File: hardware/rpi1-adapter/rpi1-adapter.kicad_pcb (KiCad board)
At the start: 2 copper layers, 17 x 35 mm, 17 parts, among them P1 I2C, P2 CONN_02X13, P3 UART, P4 CONN_02X08, P5 relays, P6 5V, U1 OPTO-TRANSISTOR-4, U2 OPTO-TRANSISTOR-4

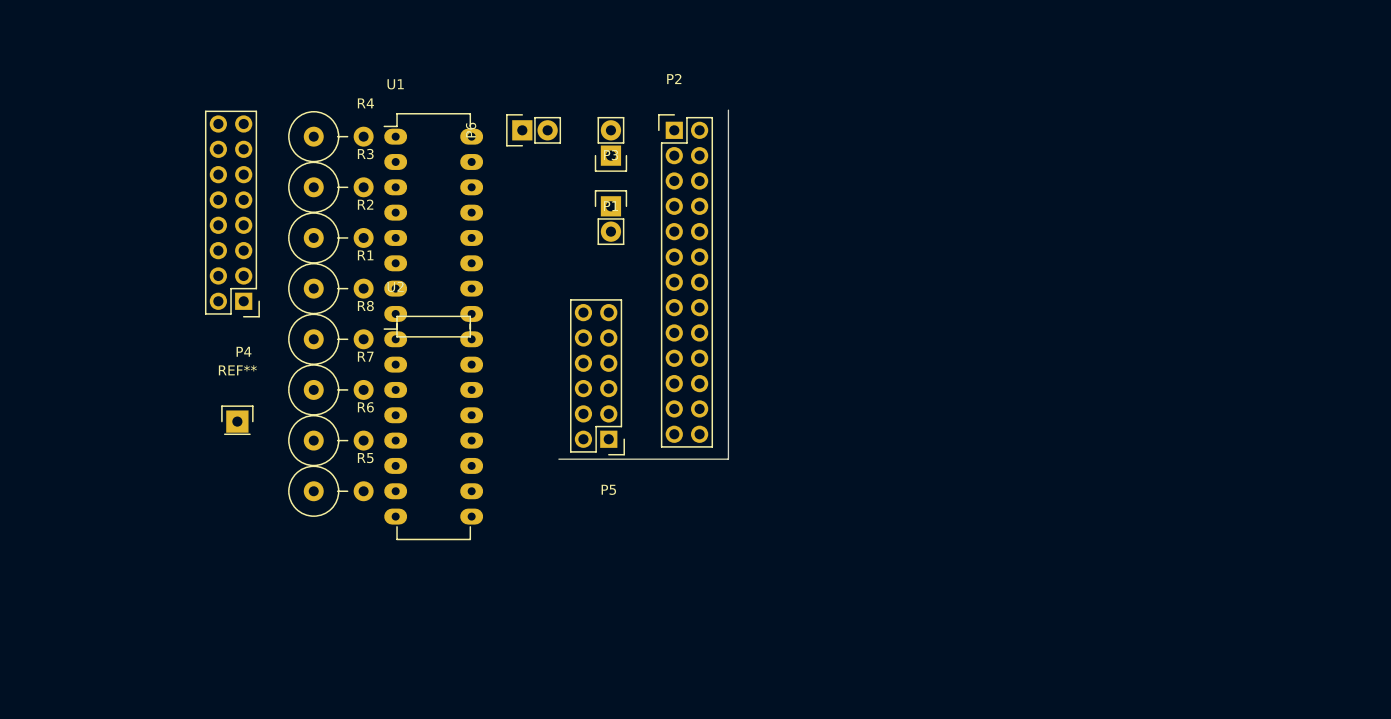
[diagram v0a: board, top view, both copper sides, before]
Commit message: o more on adapter. Add DC/DC converter to only need one 12V supply.
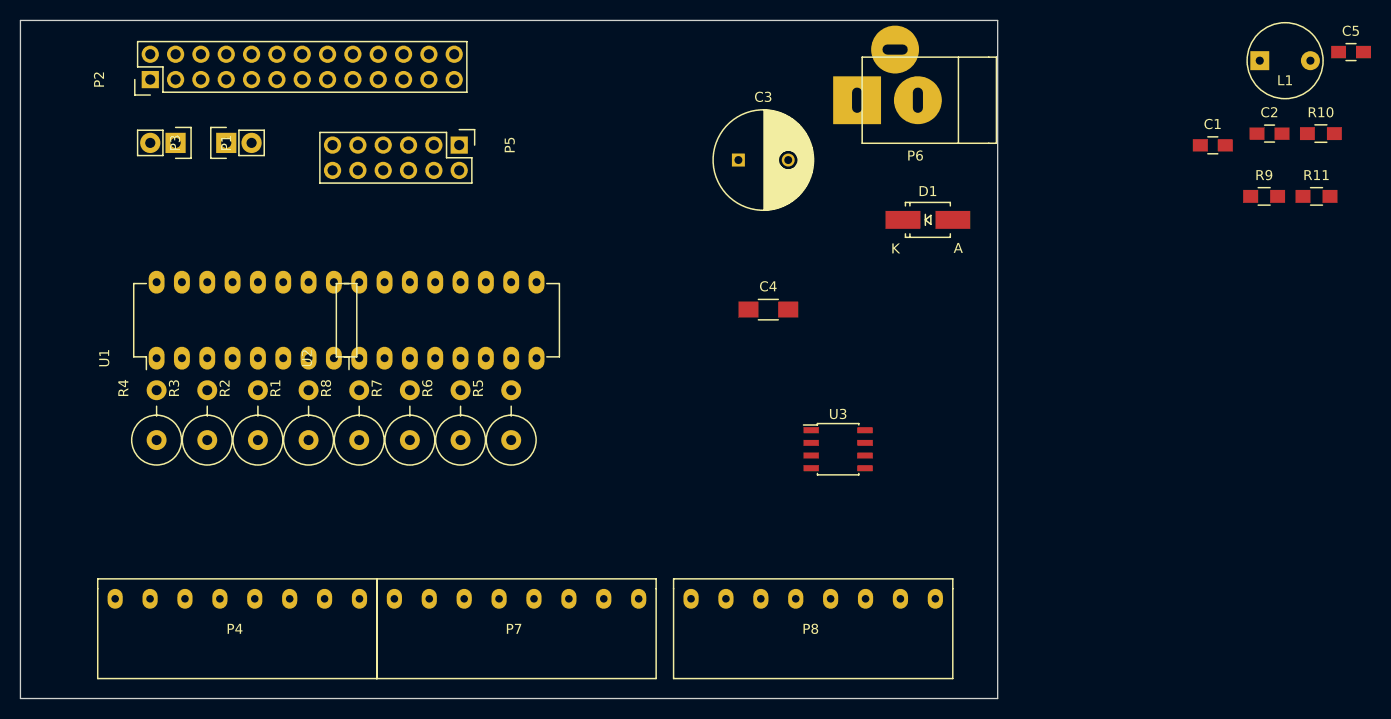
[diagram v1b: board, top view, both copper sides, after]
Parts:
- removed REF**: Pin_Header_Straight_1x01, Pin_Headers:Pin_Header_Straight_1x01
- added C1: 110p, Capacitors_SMD:C_0805_HandSoldering, F.Cu at (169.6, 34.5)
- added C2: 100n, Capacitors_SMD:C_0805_HandSoldering, F.Cu at (175.3, 33.3)
- added C3: 100u, Capacitors_ThroughHole:C_Radial_D10_L16_P5, F.Cu at (122.0, 36.0)
- added C4: 100u, Capacitors_SMD:C_1206_HandSoldering, F.Cu at (125.0, 51.0)
- added C5: 100n, Capacitors_SMD:C_0805_HandSoldering, F.Cu at (183.4, 25.2)
- added D1: D_Schottky_Small, Diodes_SMD:Diode-SMA_Handsoldering, F.Cu at (141.0, 42.0)
- added L1: L_Small, Inductors:INDUCTOR_V, F.Cu at (176.8, 26.0)
- added P7: CONN_01X08, terminal:TerminalBlock-8pin-3.5mm, F.Cu at (99.8, 80.0)
- added P8: CONN_01X08, terminal:TerminalBlock-8pin-3.5mm, F.Cu at (129.5, 80.0)
- added R10: 1k, Resistors_SMD:R_0805_HandSoldering, F.Cu at (180.4, 33.3)
- added R11: 3k, Resistors_SMD:R_0805_HandSoldering, F.Cu at (180.0, 39.6)
- added R9: 0R3, Resistors_SMD:R_0805_HandSoldering, F.Cu at (174.7, 39.6)
- added U3: MC34063, Housings_SOIC:SOIC-8_3.9x4.9mm_Pitch1.27mm, F.Cu at (132.0, 65.0)
- P4: value CONN_02X08 -> CONN_01X08; footprint Pin_Headers:Pin_Header_Straight_2x08 -> terminal:TerminalBlock-8pin-3.5mm
- P6: value 5V -> 12V; footprint Pin_Headers:Pin_Header_Straight_1x02 -> Connect:JACK_ALIM
- moved P2 52.8 mm to (63.0, 27.9), turned to 90 degrees
- moved P1 43.7 mm to (65.6, 34.3), turned to 270 degrees
- moved P6 39.8 mm to (140.0, 30.0), turned to 180 degrees
- moved P3 39.1 mm to (70.6, 34.3), turned to 90 degrees
- moved R4 33.4 mm to (63.7, 61.6), turned to 90 degrees
- moved P5 33.1 mm to (94.0, 34.5), turned to 270 degrees
- moved U1 32.7 mm to (63.7, 55.9), turned to 90 degrees
- moved P4 29.8 mm to (71.8, 80.0), turned to 0 degrees
- moved R3 26.4 mm to (68.7, 61.6), turned to 90 degrees
- moved R2 19.5 mm to (73.8, 61.6), turned to 90 degrees
- moved R5 18.9 mm to (99.2, 61.6), turned to 90 degrees
- moved R1 13.0 mm to (78.9, 61.6), turned to 90 degrees
- moved R6 12.5 mm to (94.1, 61.6), turned to 90 degrees
- moved R8 7.88 mm to (84.0, 61.6), turned to 90 degrees
- moved R7 7.57 mm to (89.1, 61.6), turned to 90 degrees
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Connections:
- P4 pad 1: Net-(P4-Pad1) -> GND
- P4 pad 2: GND -> Net-(P4-Pad2)
- P4 pad 3: Net-(P4-Pad3) -> GND
- P4 pad 4: GND -> Net-(P4-Pad4)
- P4 pad 5: Net-(P4-Pad5) -> GND
- P4 pad 6: GND -> Net-(P4-Pad6)
- P4 pad 7: Net-(P4-Pad7) -> GND
- P4 pad 8: GND -> Net-(P4-Pad8)
- P6 pad 2: +5V -> +12V
- U1 pad 1: Net-(R4-Pad2) -> Net-(R5-Pad2)
- U1 pad 10: in-17 -> in-4
- U1 pad 12: in-4 -> in-21
- U1 pad 14: in-21 -> in-22
- U1 pad 16: in-22 -> in-17
- U1 pad 2: Net-(P4-Pad15) -> Net-(P7-Pad8)
- U1 pad 3: Net-(R3-Pad2) -> Net-(R6-Pad2)
- U1 pad 4: Net-(P4-Pad13) -> Net-(P7-Pad6)
- U1 pad 5: Net-(R2-Pad2) -> Net-(R7-Pad2)
- U1 pad 6: Net-(P4-Pad11) -> Net-(P7-Pad4)
- U1 pad 7: Net-(R1-Pad2) -> Net-(R8-Pad2)
- U1 pad 8: Net-(P4-Pad9) -> Net-(P7-Pad2)
- U2 pad 1: Net-(R8-Pad2) -> Net-(R1-Pad2)
- U2 pad 2: Net-(P4-Pad7) -> Net-(P4-Pad8)
- U2 pad 3: Net-(R7-Pad2) -> Net-(R2-Pad2)
- U2 pad 4: Net-(P4-Pad5) -> Net-(P4-Pad6)
- U2 pad 5: Net-(R6-Pad2) -> Net-(R3-Pad2)
- U2 pad 6: Net-(P4-Pad3) -> Net-(P4-Pad4)
- U2 pad 7: Net-(R5-Pad2) -> Net-(R4-Pad2)
- U2 pad 8: Net-(P4-Pad1) -> Net-(P4-Pad2)
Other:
- board size 17 x 35 mm -> 98 x 68 mm
